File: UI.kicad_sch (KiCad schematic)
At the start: 40 parts

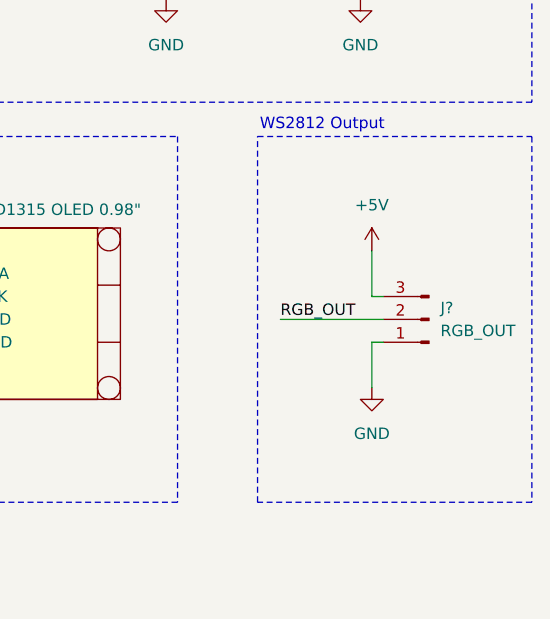
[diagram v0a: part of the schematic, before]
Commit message: Completated the Power Schema + Added Shunts resistors with OP Amp + Connected the RGB Connector to the BUCK (Fixes #5)
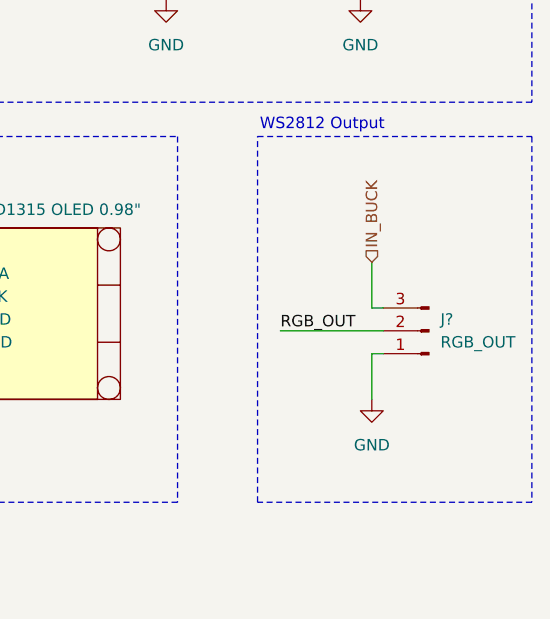
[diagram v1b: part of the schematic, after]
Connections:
- net +5V: no longer J?.3 (Pin_3)
- new net IN_BUCK: J?.3 (Pin_3)
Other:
- moved on the sheet: J?

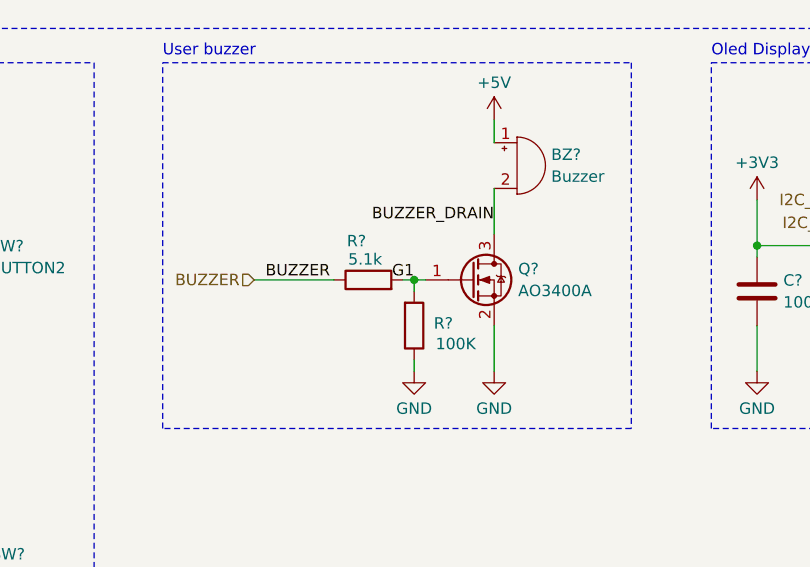
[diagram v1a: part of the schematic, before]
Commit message: Runned ERC for the first time and fixed some errors
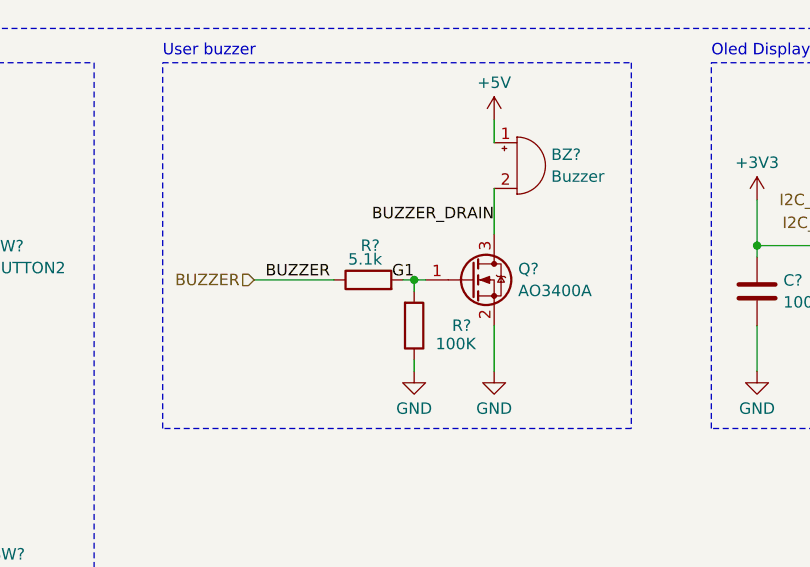
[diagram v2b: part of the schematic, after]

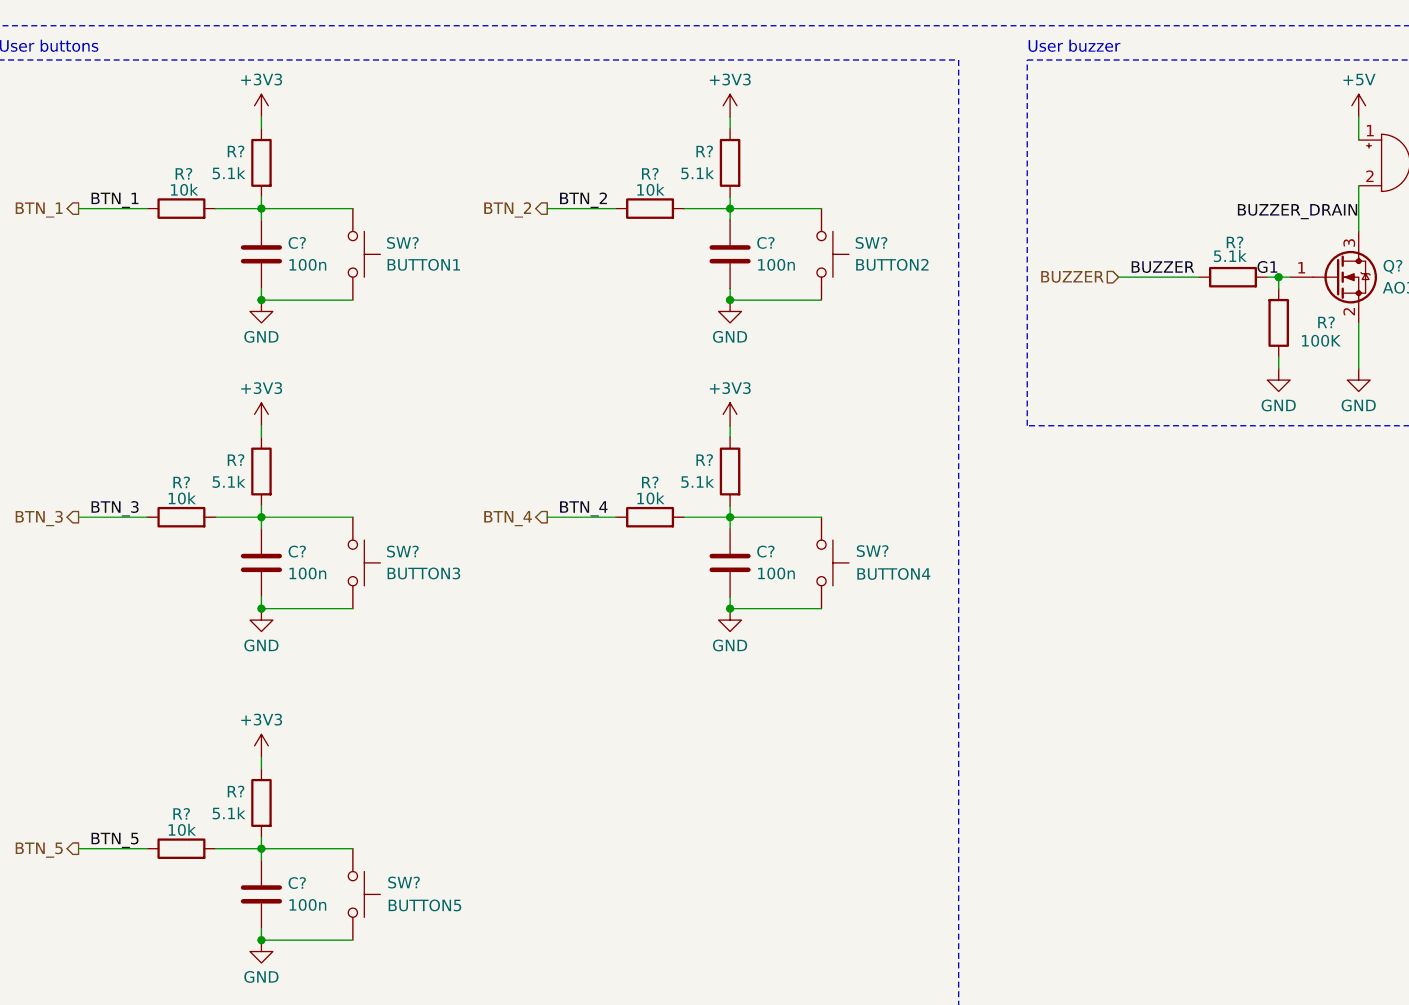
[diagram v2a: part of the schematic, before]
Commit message: Changed some value for grouping components
Basically two resistors valued 5.1k and 5K1 have the same value
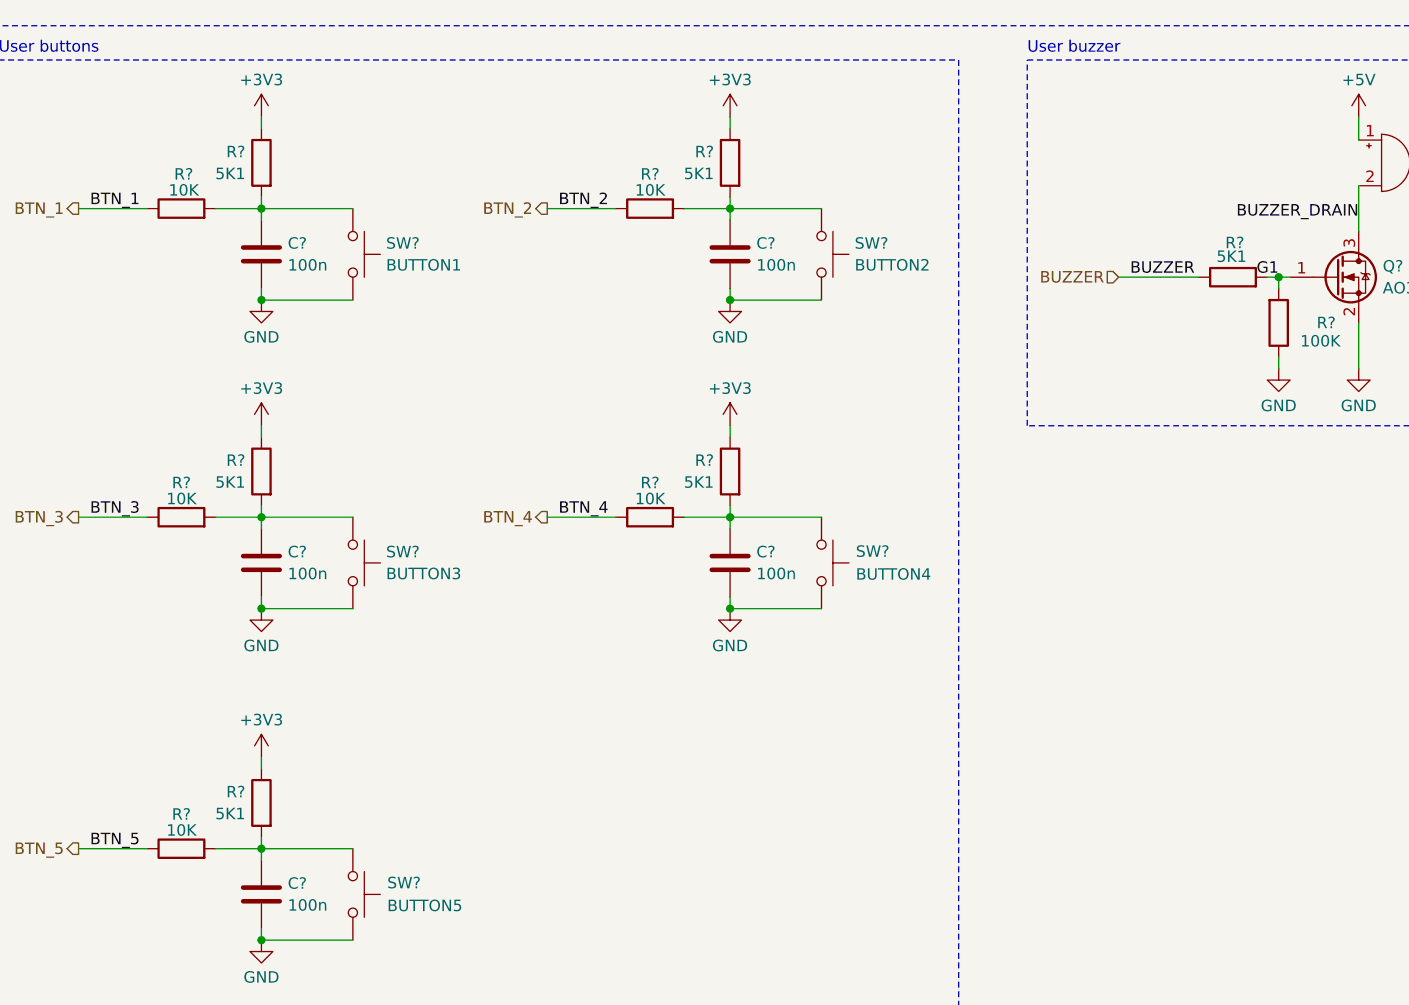
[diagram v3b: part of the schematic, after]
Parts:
- R? (x6): value 5.1k -> 5K1
- R? (x5): value 10k -> 10K
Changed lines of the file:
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@@
 			)
 		)
-		(property "Value" "5.1k"
+		(property "Value" "5K1"
 			(at 153.924 84.074 90)
 			(effects
@@
 			)
 		)
-		(property "Value" "10k"
+		(property "Value" "10K"
 			(at 87.63 110.998 90)
 			(effects
@@
 			)
 		)
-		(property "Value" "5.1k"
+		(property "Value" "5K1"
 			(at 94.742 74.8753 0)
 			(effects
@@
 			)
 		)
-		(property "Value" "5.1k"
+		(property "Value" "5K1"
 			(at 42.672 145.9953 0)
 			(effects
@@
 			)
 		)
-		(property "Value" "10k"
+		(property "Value" "10K"
 			(at 87.63 76.708 90)
 			(effects
@@
 			)
 		)
-		(property "Value" "5.1k"
+		(property "Value" "5K1"
 			(at 42.672 74.8753 0)
 			(effects
@@
 			)
 		)
-		(property "Value" "10k"
+		(property "Value" "10K"
 			(at 35.56 110.998 90)
 			(effects
@@
 			)
 		)
-		(property "Value" "10k"
+		(property "Value" "10K"
 			(at 35.56 147.828 90)
 			(effects
@@
 			)
 		)
-		(property "Value" "5.1k"
+		(property "Value" "5K1"
 			(at 94.742 109.1653 0)
 			(effects
@@
 			)
 		)
-		(property "Value" "10k"
+		(property "Value" "10K"
 			(at 35.814 76.708 90)
 			(effects
@@
 			)
 		)
-		(property "Value" "5.1k"
+		(property "Value" "5K1"
 			(at 42.672 109.1653 0)
 			(effects

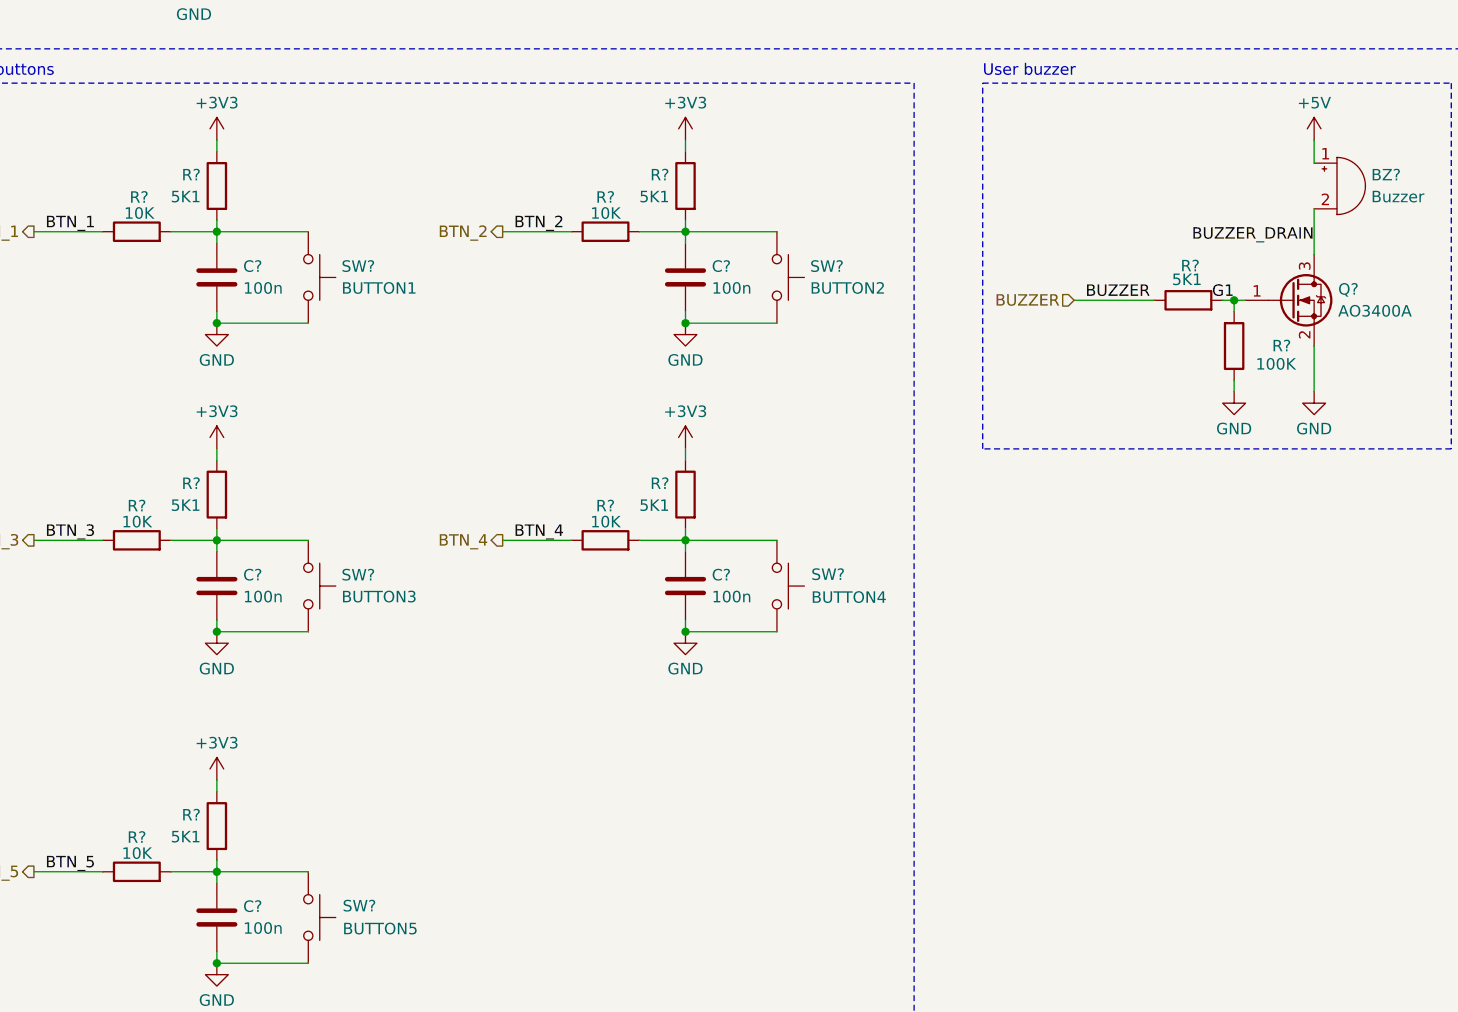
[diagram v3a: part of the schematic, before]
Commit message: Fixed some schematic issues
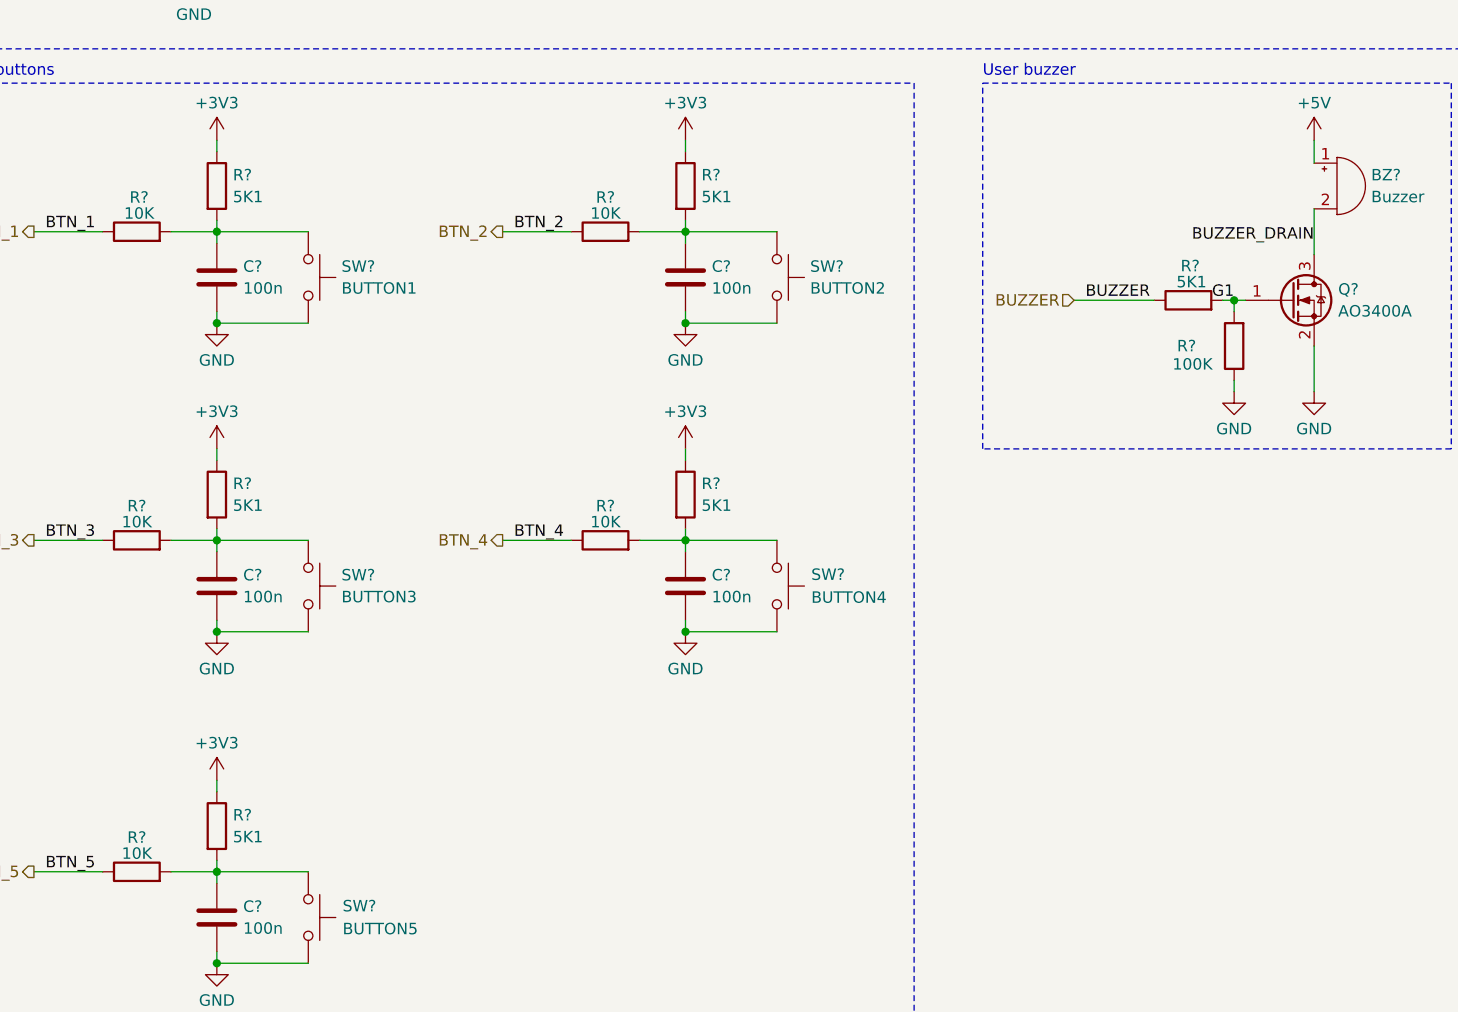
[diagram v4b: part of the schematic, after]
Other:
- moved on the sheet: R?
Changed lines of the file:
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@@
 		)
 		(property "Value" "5K1"
-			(at 153.924 84.074 90)
+			(at 154.432 84.328 90)
 			(effects
 				(font
@@
 		(lib_id "Device:R")
 		(at 96.52 73.66 0)
-		(mirror y)
 		(unit 1)
 		(exclude_from_sim no)
@@
 		(dnp no)
 		(property "Reference" "R?"
-			(at 94.742 72.4446 0)
+			(at 98.298 72.4446 0)
 			(effects
 				(font
@@
 		)
 		(property "Value" "5K1"
-			(at 94.742 74.8753 0)
+			(at 98.298 74.8753 0)
 			(effects
 				(font
@@
 		)
 		(property "Footprint" "Resistor_SMD:R_0805_2012Metric_Pad1.20x1.40mm_HandSolder"
-			(at 98.298 73.66 90)
+			(at 94.742 73.66 90)
 			(effects
 				(font
@@
 		(lib_id "Device:R")
 		(at 44.45 144.78 0)
-		(mirror y)
 		(unit 1)
 		(exclude_from_sim no)
@@
 		(dnp no)
 		(property "Reference" "R?"
-			(at 42.672 143.5646 0)
+			(at 46.228 143.5646 0)
 			(effects
 				(font
@@
 		)
 		(property "Value" "5K1"
-			(at 42.672 145.9953 0)
+			(at 46.228 145.9953 0)
 			(effects
 				(font
@@
 		)
 		(property "Footprint" "Resistor_SMD:R_0805_2012Metric_Pad1.20x1.40mm_HandSolder"
-			(at 46.228 144.78 90)
+			(at 42.672 144.78 90)
 			(effects
 				(font
@@
 		(lib_id "Device:R")
 		(at 44.45 73.66 0)
-		(mirror y)
 		(unit 1)
 		(exclude_from_sim no)
@@
 		(dnp no)
 		(property "Reference" "R?"
-			(at 42.672 72.4446 0)
+			(at 46.228 72.4446 0)
 			(effects
 				(font
@@
 		)
 		(property "Value" "5K1"
-			(at 42.672 74.8753 0)
+			(at 46.228 74.8753 0)
 			(effects
 				(font
@@
 		)
 		(property "Footprint" "Resistor_SMD:R_0805_2012Metric_Pad1.20x1.40mm_HandSolder"
-			(at 46.228 73.66 90)
+			(at 42.672 73.66 90)
 			(effects
 				(font
@@
 	(symbol
 		(lib_id "Device:R")
-		(at 157.48 91.44 0)
-		(mirror x)
+		(at 157.48 91.44 180)
 		(unit 1)
 		(exclude_from_sim no)
@@
 		(dnp no)
 		(property "Reference" "R?"
-			(at 163.83 91.44 0)
+			(at 151.13 91.44 0)
 			(effects
 				(font
@@
 		)
 		(property "Value" "100K"
-			(at 164.338 93.472 0)
+			(at 150.622 93.472 0)
 			(effects
 				(font
@@
 		)
 		(property "Footprint" "Resistor_SMD:R_0805_2012Metric_Pad1.20x1.40mm_HandSolder"
-			(at 155.702 91.44 90)
+			(at 159.258 91.44 90)
 			(effects
 				(font
@@
 		(lib_id "Device:R")
 		(at 96.52 107.95 0)
-		(mirror y)
 		(unit 1)
 		(exclude_from_sim no)
@@
 		(dnp no)
 		(property "Reference" "R?"
-			(at 94.742 106.7346 0)
+			(at 98.298 106.7346 0)
 			(effects
 				(font
@@
 		)
 		(property "Value" "5K1"
-			(at 94.742 109.1653 0)
+			(at 98.298 109.1653 0)
 			(effects
 				(font
@@
 		)
 		(property "Footprint" "Resistor_SMD:R_0805_2012Metric_Pad1.20x1.40mm_HandSolder"
-			(at 98.298 107.95 90)
+			(at 94.742 107.95 90)
 			(effects
 				(font
@@
 		(lib_id "Device:R")
 		(at 44.45 107.95 0)
-		(mirror y)
 		(unit 1)
 		(exclude_from_sim no)
@@
 		(dnp no)
 		(property "Reference" "R?"
-			(at 42.672 106.7346 0)
+			(at 46.228 106.7346 0)
 			(effects
 				(font
@@
 		)
 		(property "Value" "5K1"
-			(at 42.672 109.1653 0)
+			(at 46.228 109.1653 0)
 			(effects
 				(font
@@
 		)
 		(property "Footprint" "Resistor_SMD:R_0805_2012Metric_Pad1.20x1.40mm_HandSolder"
-			(at 46.228 107.95 90)
+			(at 42.672 107.95 90)
 			(effects
 				(font
